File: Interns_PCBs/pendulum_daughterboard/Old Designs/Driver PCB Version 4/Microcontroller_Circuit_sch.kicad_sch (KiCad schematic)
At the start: 7 parts, among them J1 AVR-ISP-6, SW1 SW_Push, U7 ATtiny85-20S

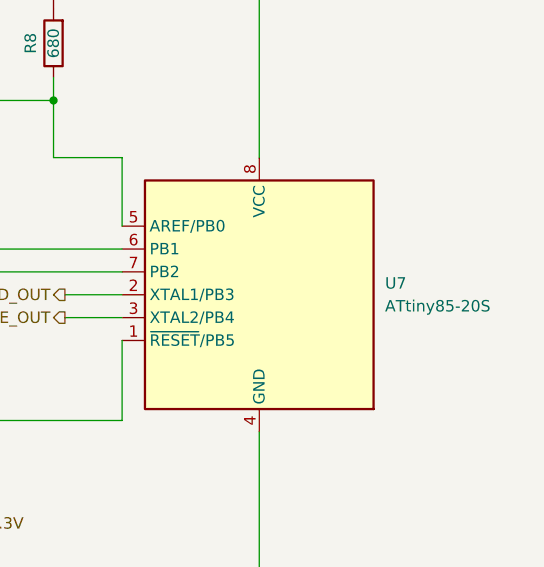
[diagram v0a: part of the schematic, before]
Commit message: Level Shifting Daughterboard
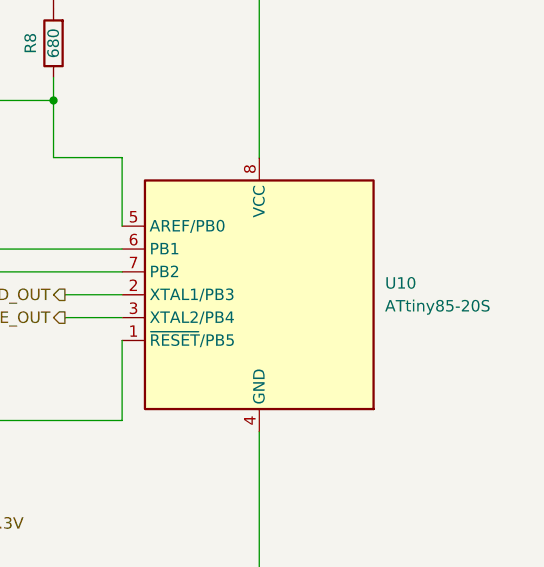
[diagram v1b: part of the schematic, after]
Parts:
- renumbered U7 to U10
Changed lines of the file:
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@@
   (symbol (lib_id "MCU_Microchip_ATtiny:ATtiny85-20S") (at 190.5 87.63 0) (mirror y) (unit 1)
     (in_bom yes) (on_board yes) (fields_autoplaced)
-    (property "Reference" "U7" (id 0) (at 204.47 86.3599 0)
+    (property "Reference" "U10" (id 0) (at 204.47 86.3599 0)
       (effects (font (size 1.27 1.27)) (justify right))
     )
